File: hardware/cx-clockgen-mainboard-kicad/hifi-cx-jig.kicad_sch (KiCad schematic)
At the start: 10 parts, among them J1 Conn_Coaxial, J2 Conn_01x01_Pin, J3 Conn_01x01_Pin, J4 Conn_01x01_Pin, J5 Conn_01x01_Pin

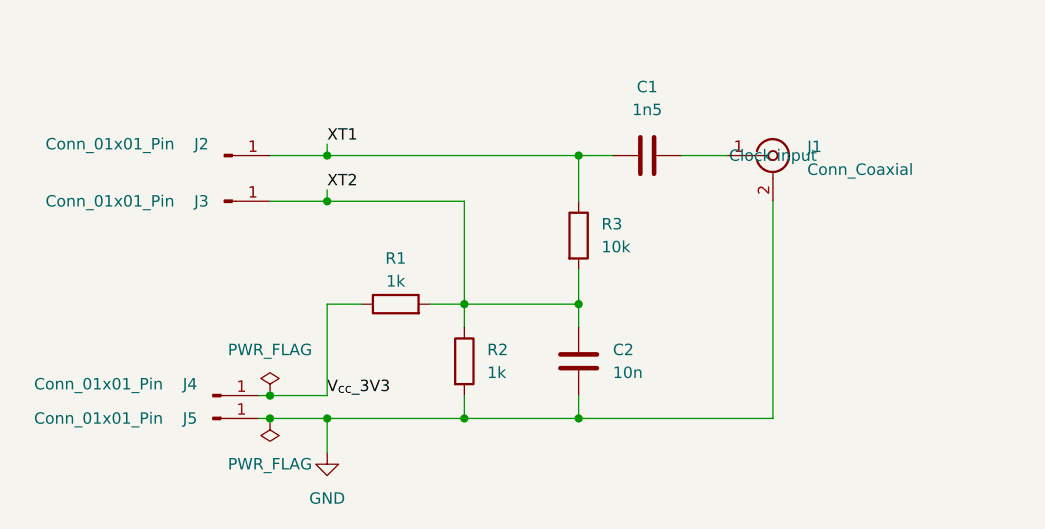
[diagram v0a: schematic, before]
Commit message: Remove obsolete KiCad project files for the clock generator main board, including DRC, ERC, DRU, PCB, schematic, and project configuration files. Updated the CX Jig project files with new author and company details, modified component properties, and adjusted net definitions for improved clarity and organization.
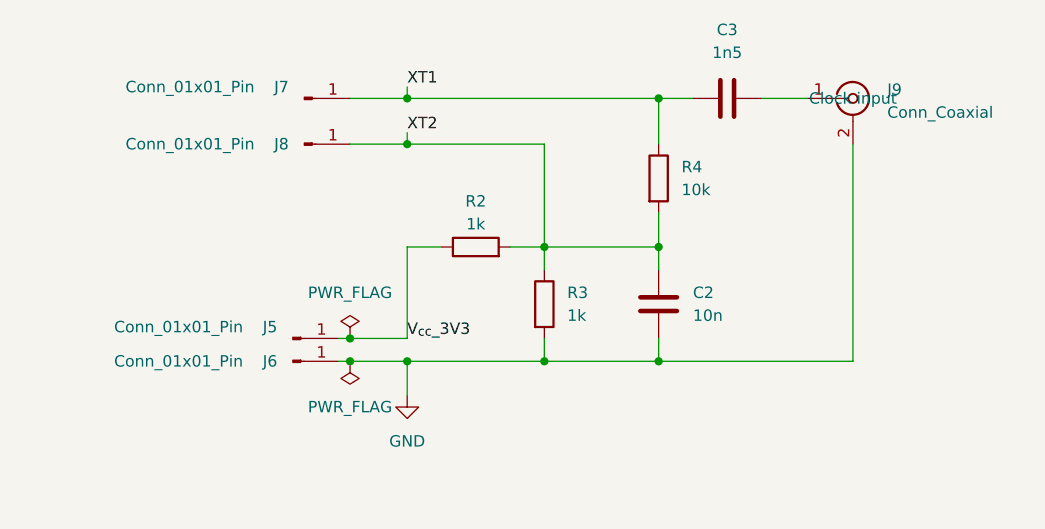
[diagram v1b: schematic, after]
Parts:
- renumbered C1 to C3, J4 to J5, J5 to J6, J2 to J7, J3 to J8, J1 to J9, R1 to R2, R2 to R3, R3 to R4
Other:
- company: ${proj-author} -> ${proj-company}
- title: ${proj-title} -> HiFi Audio CX Jig
- moved on the sheet: C2, C3, J5, J6, J7, J8, J9, R2, R3, R4
